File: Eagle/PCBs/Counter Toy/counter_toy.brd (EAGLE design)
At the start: 63.5 x 129.5 mm, 210 parts, among them Q1 2N7002, Q10 2N7002, Q100 2N7002, Q101 2N7002, Q102 2N7002, Q103 2N7002, Q104 2N7002, Q105 2N7002, Q106 2N7002, Q126 2N7002, Q127 2N7002, Q128 2N7002, Q129 2N7002, Q13 2N7002, Q130 2N7002, Q131 2N7002, Q132 2N7002, Q133 2N7002, Q134 2N7002, Q135 2N7002, Q136 2N7002, Q137 2N7002, Q138 2N7002, Q139 2N7002, Q14 2N7002, Q140 2N7002, Q141 2N7002, Q142 2N7002, Q15 2N7002, Q16 2N7002, Q162 2N7002, Q163 2N7002, Q164 2N7002, Q165 2N7002, Q166 2N7002, Q167 2N7002, Q168 2N7002, Q169 2N7002, Q17 2N7002, Q170 2N7002, Q171 2N7002, Q172 2N7002, Q173 2N7002, Q174 2N7002, Q175 2N7002, Q176 2N7002, Q177 2N7002, Q178 2N7002, Q198 2N7002, Q199 2N7002, Q200 2N7002, Q201 2N7002, Q202 2N7002, Q203 2N7002, Q204 2N7002, Q205 2N7002, Q206 2N7002, Q207 2N7002, Q208 2N7002, Q209 2N7002, Q21 2N7002, Q210 2N7002, Q211 2N7002, Q212 2N7002, Q213 2N7002, Q214 2N7002, Q22 2N7002, Q23 2N7002, Q234 2N7002, Q235 2N7002, Q236 2N7002, Q237 2N7002, Q238 2N7002, Q239 2N7002, Q240 2N7002, Q241 2N7002, Q242 2N7002, Q243 2N7002, Q244 2N7002, Q245 2N7002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

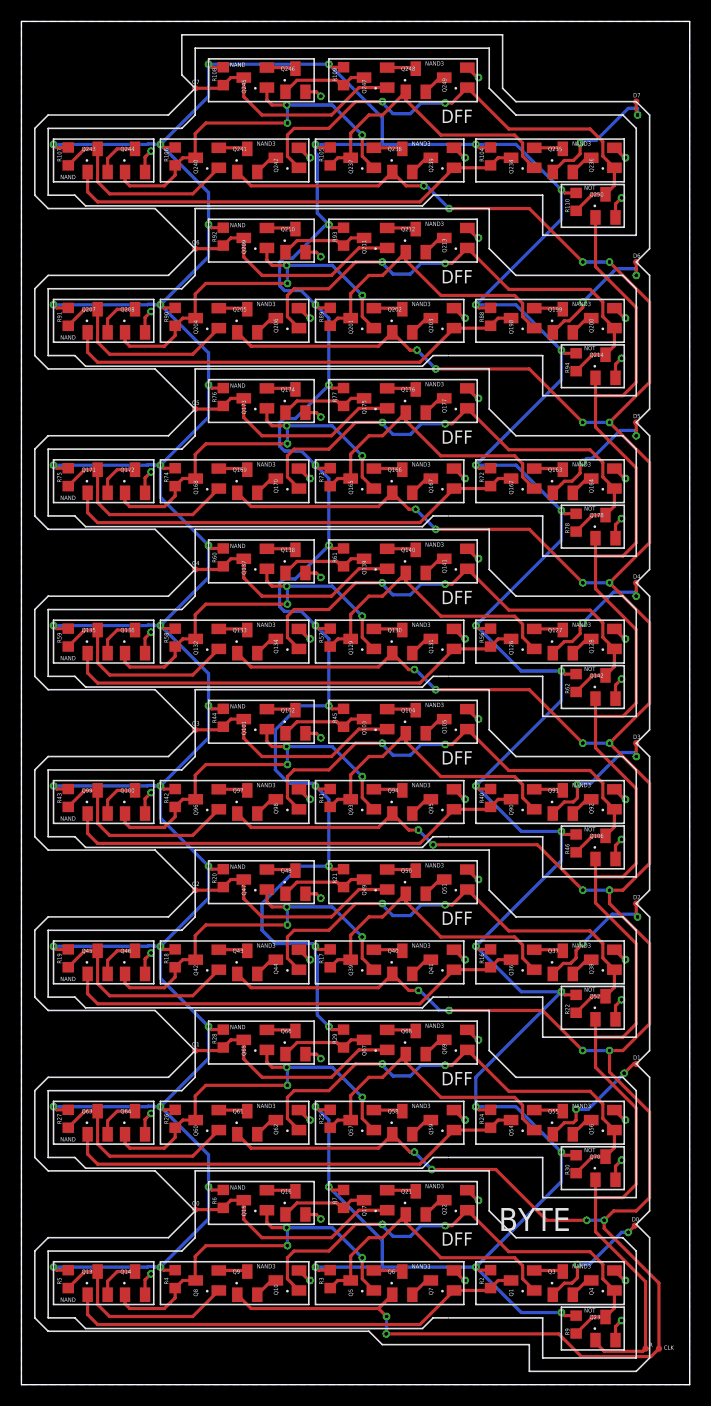
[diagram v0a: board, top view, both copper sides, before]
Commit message: Made DFF and byte more compact
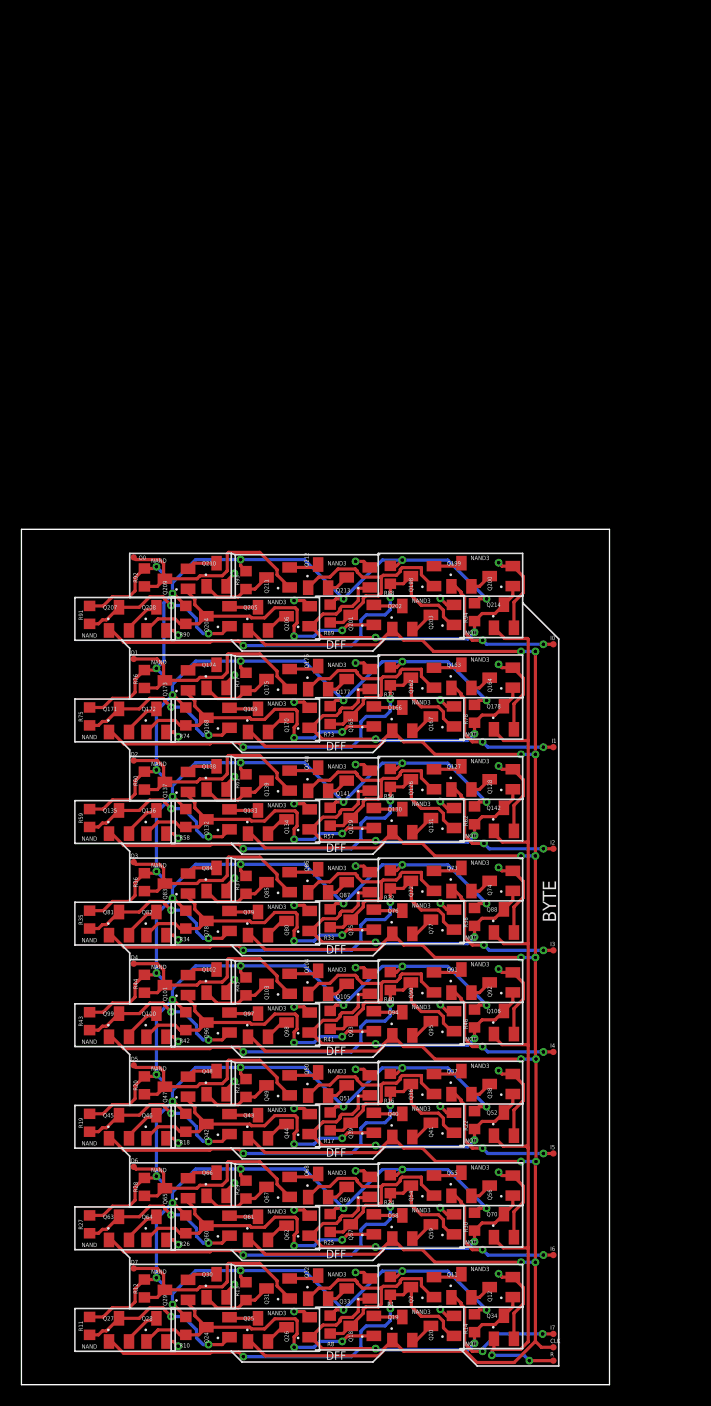
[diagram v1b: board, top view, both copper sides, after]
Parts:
- removed D0, D1, D2, D3, D4, D5, D6, D7: TPPAD6, ellajameson-core:TP06R
- removed Q1, Q10, Q13, Q14, Q15, Q16, Q17, Q21, Q22, Q23, Q234, Q235, Q236, Q237, Q238, Q239, Q240, Q241, Q242, Q243, Q244, Q245, Q246, Q247, Q248, Q249, Q250, Q3, Q4, Q5, Q6, Q7, Q8, Q9: 2N7002, ellajameson-core:SOT23
- removed R104, R105, R106, R107, R108, R109, R110, R2, R3, R4, R5, R6, R7, R9: (no value), ellajameson-core:R0603
- added I0, I1, I2, I3, I4, I5, I6, I7: TPPAD6, ellajameson-core:TP06R
- added Q11, Q12, Q18, Q19, Q2, Q20, Q24, Q25, Q26, Q27, Q28, Q29, Q30, Q31, Q32, Q33, Q34, Q72, Q73, Q74, Q75, Q76, Q77, Q78, Q79, Q80, Q81, Q82, Q83, Q84, Q85, Q86, Q87, Q88: 2N7002, ellajameson-core:SOT23
- added R1, R10, R11, R12, R13, R14, R32, R33, R34, R35, R36, R37, R38, R8: (no value), ellajameson-core:R0603
- moved O7 112.3 mm to (10.7, 11.0)
- moved O6 87.4 mm to (10.7, 20.7)
- moved O5 62.6 mm to (10.7, 30.4)
- moved O0 62.3 mm to (10.7, 78.6)
- moved O4 37.9 mm to (10.7, 40.0)
- moved O1 37.7 mm to (10.7, 69.0)
- moved R93 33.9 mm to (21.3, 76.5)
- moved Q211 33.6 mm to (24.4, 76.7)
- moved Q213 33.6 mm to (32.0, 76.7)
- moved R92 33.2 mm to (11.7, 76.7)
- moved Q209 33.2 mm to (14.7, 76.6)
- moved Q212 33.2 mm to (28.2, 76.8)
- moved Q210 32.6 mm to (18.5, 77.0)
- moved R77 28.6 mm to (21.3, 66.8)
- moved Q207 28.4 mm to (9.27, 72.8)
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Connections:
- removed net N$12: CLK.TP, Q130.1, Q133.1, Q166.1, Q169.1, Q202.1, Q205.1, Q238.1, Q241.1, Q40.1, Q43.1, Q58.1, Q6.1, Q61.1, Q9.1, Q94.1, Q97.1
- removed net N$13: Q5.2, Q6.3
- removed net N$15: Q6.2, Q7.3
- removed net N$16: Q8.2, Q9.3
- removed net N$18: Q10.1, Q22.1, Q23.3, Q4.1, R9.1
- removed net N$2: Q1.1, Q21.1, Q5.3, R3.1
- removed net N$20: Q10.3, Q9.2
- removed net N$261: Q234.1, Q237.3, Q248.1, R105.1
- removed net N$262: Q234.3, Q239.1, Q243.1, R104.1
- removed net N$263: D7.TP, Q235.1
- removed net N$264: Q234.2, Q235.3
- removed net N$265: Q235.2, Q236.3
- removed net N$266: Q237.1, Q240.3, Q244.1, Q245.1, R106.1
- removed net N$268: Q237.2, Q238.3
- removed net N$269: Q238.2, Q239.3
- removed net N$270: Q240.2, Q241.3
- removed net N$271: Q236.1, Q242.1, Q249.1, Q250.3, R110.1
- removed net N$272: Q241.2, Q242.3
- removed net N$273: Q240.1, Q243.3, R107.1
- removed net N$274: Q243.2, Q244.3
- removed net N$275: Q245.2, Q246.3
- removed net N$276: O7.TP, Q245.3, Q247.1, R108.1
- removed net N$277: Q246.1, Q247.3, R109.1
- removed net N$278: Q247.2, Q248.3
- removed net N$279: Q248.2, Q249.3
- removed net N$28: Q13.3, Q8.1, R5.1
- removed net N$29: Q13.2, Q14.3
- removed net N$30: Q15.2, Q16.3
- removed net N$34: O0.TP, Q15.3, Q17.1, R6.1
- removed net N$37: Q16.1, Q17.3, R7.1
- removed net N$38: Q17.2, Q21.3
- removed net N$39: Q21.2, Q22.3
- removed net N$40: Q106.1, Q142.1, Q178.1, Q214.1, Q23.1, Q250.1, Q52.1, Q70.1, R.TP
- removed net N$5: Q1.3, Q13.1, Q7.1, R2.1
- removed net N$6: D0.TP, Q3.1
- removed net N$7: Q1.2, Q3.3
- removed net N$8: Q3.2, Q4.3
- removed net N$9: Q14.1, Q15.1, Q5.1, Q8.3, R4.1
- new net N$1: Q18.3, Q2.1, Q32.1, R8.1
- new net N$10: Q11.3, Q2.2
- new net N$11: Q11.2, Q12.3
- new net N$14: Q18.1, Q24.3, Q28.1, Q29.1, R10.1
- new net N$17: CLK.TP, Q130.1, Q133.1, Q166.1, Q169.1, Q19.1, Q202.1, Q205.1, Q25.1, Q40.1, Q43.1, Q58.1, Q61.1, Q76.1, Q79.1, Q94.1, Q97.1
- new net N$19: Q18.2, Q19.3
- new net N$21: Q19.2, Q20.3
- new net N$22: Q24.2, Q25.3
- new net N$23: Q12.1, Q26.1, Q33.1, Q34.3, R14.1
- new net N$24: Q25.2, Q26.3
- new net N$25: Q24.1, Q27.3, R11.1
- new net N$26: Q27.2, Q28.3
- new net N$27: Q29.2, Q30.3
- new net N$3: Q2.3, Q20.1, Q27.1, R1.1
- new net N$31: O7.TP, Q29.3, Q31.1, R12.1
- new net N$32: Q30.1, Q31.3, R13.1
- new net N$33: Q31.2, Q32.3
- new net N$35: Q32.2, Q33.3
- new net N$36: Q106.1, Q142.1, Q178.1, Q214.1, Q34.1, Q52.1, Q70.1, Q88.1, R.TP
- new net N$4: I7.TP, Q11.1
- new net N$81: Q72.1, Q75.3, Q86.1, R33.1
- new net N$82: Q72.3, Q77.1, Q81.1, R32.1
- new net N$83: I3.TP, Q73.1
- new net N$84: Q72.2, Q73.3
- new net N$85: Q73.2, Q74.3
- new net N$86: Q75.1, Q78.3, Q82.1, Q83.1, R34.1
- new net N$88: Q75.2, Q76.3
- new net N$89: Q76.2, Q77.3
- new net N$90: Q78.2, Q79.3
- new net N$91: Q74.1, Q80.1, Q87.1, Q88.3, R38.1
- new net N$92: Q79.2, Q80.3
- new net N$93: Q78.1, Q81.3, R35.1
- new net N$94: Q81.2, Q82.3
- new net N$95: Q83.2, Q84.3
- new net N$96: O3.TP, Q83.3, Q85.1, R36.1
- new net N$97: Q84.1, Q85.3, R37.1
- new net N$98: Q85.2, Q86.3
- new net N$99: Q86.2, Q87.3
- net GND: now also Q12.2, Q20.2, Q26.2, Q28.2, Q30.2, Q33.2, Q34.2, Q74.2, Q77.2, Q80.2, Q82.2, Q84.2, Q87.2, Q88.2; no longer Q10.2, Q14.2, Q16.2, Q22.2, Q23.2, Q236.2, Q239.2, Q242.2, Q244.2, Q246.2, Q249.2, Q250.2, Q4.2, Q7.2
- net N$103: now also I4.TP; no longer D3.TP
- net N$116: now also O4.TP; no longer O3.TP
- net N$143: now also I2.TP; no longer D4.TP
- net N$156: now also O2.TP; no longer O4.TP
- net N$183: now also I1.TP; no longer D5.TP
- net N$196: now also O1.TP; no longer O5.TP
- net N$223: now also I0.TP; no longer D6.TP
- net N$236: now also O0.TP; no longer O6.TP
- net N$43: now also I5.TP; no longer D2.TP
- net N$56: now also O5.TP; no longer O2.TP
- net N$63: now also I6.TP; no longer D1.TP
- net N$76: now also O6.TP; no longer O1.TP
- net VCC: now also R1.2, R10.2, R11.2, R12.2, R13.2, R14.2, R32.2, R33.2, R34.2, R35.2, R36.2, R37.2, R38.2, R8.2; no longer R104.2, R105.2, R106.2, R107.2, R108.2, R109.2, R110.2, R2.2, R3.2, R4.2, R5.2, R6.2, R7.2, R9.2
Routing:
- net N$12: track 451.2 -> 0.00 mm, vias 30 -> 0
- net N$17: track 0.00 -> 304.6 mm, vias 0 -> 14
- net VCC: track 675.0 -> 489.4 mm, vias 56 -> 48
- net N$40: track 154.1 -> 0.00 mm
- net N$36: track 0.00 -> 104.5 mm, vias 0 -> 2
- net N$271: track 47.8 -> 0.00 mm, vias 2 -> 0
- net N$18: track 47.8 -> 0.00 mm, vias 2 -> 0
- net N$5: track 44.4 -> 0.00 mm
- net N$262: track 44.4 -> 0.00 mm
- net N$82: track 0.00 -> 41.9 mm, vias 0 -> 2
- net N$3: track 0.00 -> 41.9 mm, vias 0 -> 2
- net N$266: track 37.8 -> 0.00 mm, vias 3 -> 0
- net N$9: track 37.8 -> 0.00 mm, vias 3 -> 0
- net GND: track 94.2 -> 126.7 mm, vias 56 -> 48
- net N$91: track 0.00 -> 30.9 mm, vias 0 -> 2
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- removed copper zone on layer 16, net GND
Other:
- board size 63.5 x 129.5 mm -> 55.9 x 81.3 mm

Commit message: Update counter_toy.brd
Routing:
- added copper zone on layer 16, net GND
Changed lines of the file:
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@@
 </layers>
 <board>
-<fusionsync huburn="a.cGVyc29uYWw6dWUyZGY0M2Ex" projecturn="a.cGVyc29uYWw6dWUyZGY0M2ExIzIwMjEwMTIwMzczOTE5OTMx" f3durn="urn:adsk.wipprod:dm.lineage:RKQa1e1pTIef6ifPqg5Tig" pcbguid="" lastpulledtime="" lastsyncedchangeguid="" latestrevisionid="468e08d1-bdf0-40c3-9270-53415b291e36" lastsyncedrevisionid="468e08d1-bdf0-40c3-9270-53415b291e36" lastboardhashguid="1fa0f9e9-e586-e5ba-25a4-847b196b3b5a" lastpushedtime="2023-04-18T12:42:12Z" linktopcb3d="true"/>
+<fusionsync huburn="a.cGVyc29uYWw6dWUyZGY0M2Ex" projecturn="a.cGVyc29uYWw6dWUyZGY0M2ExIzIwMjEwMTIwMzczOTE5OTMx" f3durn="urn:adsk.wipprod:dm.lineage:RKQa1e1pTIef6ifPqg5Tig" pcbguid="" lastpulledtime="" lastsyncedchangeguid="" latestrevisionid="ae0b7da3-c6b2-42a1-a777-f11f63b34cd7" lastsyncedrevisionid="ae0b7da3-c6b2-42a1-a777-f11f63b34cd7" lastboardhashguid="42e16079-18b1-1462-3737-b46bbdbd1827" lastpushedtime="2023-04-19T04:21:05Z" linktopcb3d="true"/>
 <plain>
 <wire x1="33.909" y1="11.43" x2="47.625" y2="11.43" width="0.1524" layer="21"/>
@@
 <wire x1="40.4249625" y1="74.102" x2="39.7995625" y2="74.7274" width="0.3048" layer="1"/>
 <via x="39.7995625" y="74.7274" extent="1-16" drill="0.35"/>
-<wire x1="45.339" y1="68.453" x2="46.797" y2="71.925" width="0" layer="19" extent="1-1"/>
-<wire x1="45.339" y1="58.801" x2="46.797" y2="62.273" width="0" layer="19" extent="1-1"/>
-<wire x1="45.339" y1="49.149" x2="46.797" y2="52.621" width="0" layer="19" extent="1-1"/>
-<wire x1="45.339" y1="39.497" x2="46.797" y2="42.969" width="0" layer="19" extent="1-1"/>
-<wire x1="45.339" y1="29.845" x2="46.797" y2="33.317" width="0" layer="19" extent="1-1"/>
-<wire x1="45.339" y1="20.193" x2="46.797" y2="23.665" width="0" layer="19" extent="1-1"/>
-<wire x1="45.339" y1="10.541" x2="46.797" y2="14.013" width="0" layer="19" extent="1-1"/>
-<wire x1="41.105" y1="74.102" x2="45.339" y2="78.105" width="0" layer="19" extent="1-1"/>
-<wire x1="41.105" y1="64.45" x2="45.339" y2="68.453" width="0" layer="19" extent="1-1"/>
-<wire x1="41.105" y1="54.798" x2="45.339" y2="58.801" width="0" layer="19" extent="1-1"/>
-<wire x1="41.105" y1="45.146" x2="45.339" y2="49.149" width="0" layer="19" extent="1-1"/>
-<wire x1="41.105" y1="35.494" x2="45.339" y2="39.497" width="0" layer="19" extent="1-1"/>
-<wire x1="41.105" y1="25.842" x2="45.339" y2="29.845" width="0" layer="19" extent="1-1"/>
-<wire x1="41.105" y1="16.19" x2="45.339" y2="20.193" width="0" layer="19" extent="1-1"/>
-<wire x1="41.105" y1="6.538" x2="45.339" y2="10.541" width="0" layer="19" extent="1-1"/>
-<wire x1="33.104" y1="77.658" x2="39.7995625" y2="74.7274" width="0" layer="19" extent="1-1"/>
-<wire x1="27.389" y1="73.975" x2="31.75" y2="78.232" width="0" layer="19" extent="1-1"/>
-<wire x1="20.241" y1="77.089" x2="25.908" y2="74.5128" width="0" layer="19" extent="1-1"/>
-<wire x1="14.90041875" y1="71.2222" x2="19.492" y2="75.862" width="0" layer="19" extent="1-1"/>
-<wire x1="20.241" y1="67.437" x2="14.90041875" y2="71.2222" width="0" layer="19" extent="1-1"/>
-<wire x1="25.908" y1="64.8608" x2="20.241" y2="67.437" width="0" layer="19" extent="1-1"/>
-<wire x1="31.75" y1="68.58" x2="27.389" y2="64.323" width="0" layer="19" extent="1-1"/>
-<wire x1="14.90041875" y1="61.5702" x2="19.492" y2="66.21" width="0" layer="19" extent="1-1"/>
-<wire x1="20.241" y1="57.785" x2="14.90041875" y2="61.5702" width="0" layer="19" extent="1-1"/>
-<wire x1="25.908" y1="55.2088" x2="20.241" y2="57.785" width="0" layer="19" extent="1-1"/>
-<wire x1="31.75" y1="58.928" x2="27.389" y2="54.671" width="0" layer="19" extent="1-1"/>
-<wire x1="14.90041875" y1="51.9182" x2="19.492" y2="56.558" width="0" layer="19" extent="1-1"/>
-<wire x1="20.241" y1="48.133" x2="14.90041875" y2="51.9182" width="0" layer="19" extent="1-1"/>
-<wire x1="25.908" y1="45.5568" x2="20.241" y2="48.133" width="0" layer="19" extent="1-1"/>
-<wire x1="31.75" y1="49.276" x2="27.389" y2="45.019" width="0" layer="19" extent="1-1"/>
-<wire x1="14.90041875" y1="42.2662" x2="19.492" y2="46.906" width="0" layer="19" extent="1-1"/>
-<wire x1="20.241" y1="38.481" x2="14.90041875" y2="42.2662" width="0" layer="19" extent="1-1"/>
-<wire x1="25.908" y1="35.9048" x2="20.241" y2="38.481" width="0" layer="19" extent="1-1"/>
-<wire x1="31.75" y1="39.624" x2="27.389" y2="35.367" width="0" layer="19" extent="1-1"/>
-<wire x1="14.90041875" y1="32.6142" x2="19.492" y2="37.254" width="0" layer="19" extent="1-1"/>
-<wire x1="20.241" y1="28.829" x2="14.90041875" y2="32.6142" width="0" layer="19" extent="1-1"/>
-<wire x1="25.908" y1="26.2528" x2="20.241" y2="28.829" width="0" layer="19" extent="1-1"/>
-<wire x1="31.75" y1="29.972" x2="27.389" y2="25.715" width="0" layer="19" extent="1-1"/>
-<wire x1="14.90041875" y1="22.9622" x2="19.492" y2="27.602" width="0" layer="19" extent="1-1"/>
-<wire x1="20.241" y1="19.177" x2="14.90041875" y2="22.9622" width="0" layer="19" extent="1-1"/>
-<wire x1="25.908" y1="16.6008" x2="20.241" y2="19.177" width="0" layer="19" extent="1-1"/>
-<wire x1="31.75" y1="20.32" x2="27.389" y2="16.063" width="0" layer="19" extent="1-1"/>
-<wire x1="14.90041875" y1="13.3102" x2="19.492" y2="17.95" width="0" layer="19" extent="1-1"/>
-<wire x1="20.241" y1="9.525" x2="14.90041875" y2="13.3102" width="0" layer="19" extent="1-1"/>
-<wire x1="25.908" y1="6.9488" x2="20.241" y2="9.525" width="0" layer="19" extent="1-1"/>
-<wire x1="31.75" y1="10.668" x2="27.389" y2="6.411" width="0" layer="19" extent="1-1"/>
-<wire x1="14.90041875" y1="3.6582" x2="19.492" y2="8.298" width="0" layer="19" extent="1-1"/>
+<polygon width="0.0762" layer="16">
+<vertex x="0" y="0"/>
+<vertex x="55.88" y="0"/>
+<vertex x="55.88" y="81.28"/>
+<vertex x="0" y="81.28"/>
+</polygon>
 </signal>
 <signal name="N$11">
